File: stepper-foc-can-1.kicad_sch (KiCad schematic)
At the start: 60 parts, among them J1 TC2030, J2 Conn_01x02, J4 Conn_01x04_Pin, J5 Conn_01x02, J6 Conn_01x02, M1 Stepper_Motor_bipolar, SW1 SW_Push, SW2 SW_Push, SW3 SW_Push, U1 STM32G474RBTx, U2 MX25947, U3 TPS62933, U4 AS5047P, U9 TCAN3413, Y1 Crystal_GND24

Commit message: schem: run and fix ERC
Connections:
- net BTN1: now also U1.58 (PB5)
- no-connect marks 27 -> 26
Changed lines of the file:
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@@
 		(color 0 0 0 0)
 	)
+	(junction
+		(at 38.1 191.77)
+		(diameter 0)
+		(color 0 0 0 0)
+	)
 	(no_connect
 		(at 120.65 125.73)
@@
 		(at 85.09 72.39)
 	)
-	(no_connect
-		(at 120.65 110.49)
-	)
 	(wire
 		(pts
@@
 	(wire
 		(pts
-			(xy 34.29 191.77) (xy 40.64 191.77)
+			(xy 34.29 191.77) (xy 38.1 191.77)
 		)
 		(stroke
@@
 	(wire
 		(pts
+			(xy 130.81 110.49) (xy 120.65 110.49)
+		)
+		(stroke
+			(width 0)
+			(type default)
+		)
+	)
+	(wire
+		(pts
 			(xy 71.12 41.91) (xy 71.12 43.18)
 		)
@@
 	(wire
 		(pts
+			(xy 38.1 191.77) (xy 40.64 191.77)
+		)
+		(stroke
+			(width 0)
+			(type default)
+		)
+	)
+	(wire
+		(pts
 			(xy 74.93 85.09) (xy 85.09 85.09)
 		)
@@
 		)
 	)
+	(label "BTN1"
+		(at 130.81 110.49 180)
+		(effects
+			(font
+				(size 1.27 1.27)
+			)
+			(justify right bottom)
+		)
+	)
 	(label "IN2_A"
 		(at 166.37 78.74 0)
@@
 					(unit 1)
 				)
+			)
+		)
+	)
+	(symbol
+		(lib_id "power:PWR_FLAG")
+		(at 38.1 191.77 180)
+		(unit 1)
+		(body_style 1)
+		(exclude_from_sim no)
+		(in_bom yes)
+		(on_board yes)
+		(in_pos_files yes)
+		(dnp no)
+		(fields_autoplaced yes)
+		(property "Reference" "#FLG09"
+			(at 38.1 193.675 0)
+			(hide yes)
+			(show_name no)
+			(do_not_autoplace no)
+			(effects
+				(font
+					(size 1.27 1.27)
+				)
+			)
+		)
+		(property "Value" "PWR_FLAG"
+			(at 38.1 196.85 0)
+			(hide yes)
+			(show_name no)
+			(do_not_autoplace no)
+			(effects
+				(font
+					(size 1.27 1.27)
+				)
+			)
+		)
+		(property "Footprint" ""
+			(at 38.1 191.77 0)
+			(hide yes)
+			(show_name no)
+			(do_not_autoplace no)
+			(effects
+				(font
+					(size 1.27 1.27)
+				)
+			)
+		)
+		(property "Datasheet" ""
+			(at 38.1 191.77 0)
+			(hide yes)
+			(show_name no)
+			(do_not_autoplace no)
+			(effects
+				(font
+					(size 1.27 1.27)
+				)
+			)
+		)
+		(property "Description" "Special symbol for telling ERC where power comes from"
+			(at 38.1 191.77 0)
+			(hide yes)
+			(show_name no)
+			(do_not_autoplace no)
+			(effects
+				(font
+					(size 1.27 1.27)
+				)
+			)
+		)
+		(pin "1"
+		)
+		(instances
+			(project "stepper-foc-can-1"
+				(path "/7e511d2f-8abe-4907-a647-133ba6c8a8df"
+					(reference "#FLG09")
+					(unit 1)
+				)

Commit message: schem: add missing footprints
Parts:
- M1: footprint (none) -> Connector_JST:JST_XH_S4B-XH-A_1x04_P2.50mm_Horizontal
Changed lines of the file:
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@@
 			)
 		)
-		(property "Footprint" ""
+		(property "Footprint" "Connector_JST:JST_XH_S4B-XH-A_1x04_P2.50mm_Horizontal"
 			(at 204.724 78.486 0)
 			(hide yes)

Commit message: schem: add ordering info to BOM
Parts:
- M1: now left out of the parts list
- U1: Basic (none) -> X; JLCPCB Part # (none) -> C1235414; Manufacturer (none) -> STMicroelectronics; Manufacturer Part Number (none) -> STM32G474RBT3
- U2: Basic (none) -> X; JLCPCB Part # (none) -> C5875698; Manufacturer (none) -> Wuxi Maxinmicro; Manufacturer Part Number (none) -> MX25947ES
- U4: Basic (none) -> X; JLCPCB Part # (none) -> C962063; Manufacturer (none) -> AMS; Manufacturer Part Number (none) -> AS5047P-ATSM

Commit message: schem: add title
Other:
- company: (none) -> Rémi Ait-Younes
- title: (none) -> Stepper FOC CAN 1
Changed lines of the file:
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@@
 	(generator_version "10.0")
 	(paper "A4")
+	(title_block
+		(title "Stepper FOC CAN 1")
+		(date "2026-04-11")
+		(rev "01")
+		(company "Rémi Ait-Younes")
+	)
 	(rectangle
 		(start 233.68 82.55)

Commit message: schem: reannotate
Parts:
- renumbered C3 to C1, C15 to C10, C12 to C11, C13 to C12, C14 to C13, C17 to C14, C16 to C15, C1 to C16, C2 to C17, C6 to C2, C29 to C24, C30 to C25, C24 to C26, C4 to C3, C5 to C4, C7 to C5, C9 to C6, C10 to C7, C11 to C9, D11 to D6, J4 to J3, J5 to J4, J6 to J5, JP2 to JP1, R5 to R3, R8 to R4, R4 to R5, R9 to R6, R10 to R7, R11 to R8, R13 to R9, TP4 to TP1, U9 to U4, U4 to U5

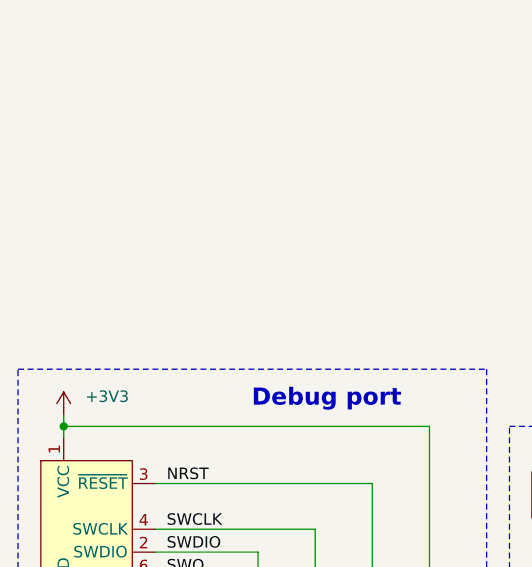
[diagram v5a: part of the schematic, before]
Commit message: schem: add mounting holes
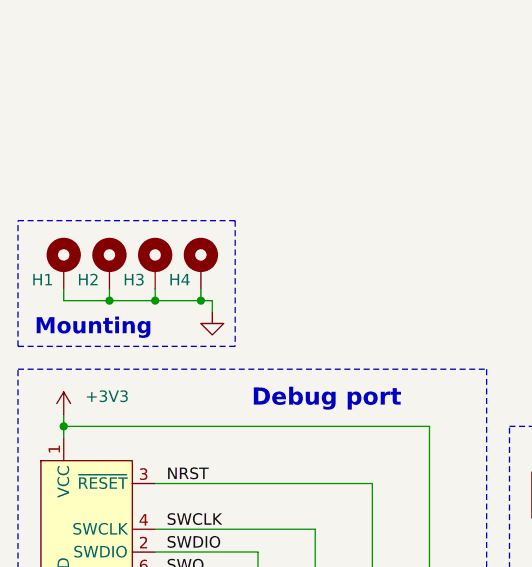
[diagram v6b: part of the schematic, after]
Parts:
- added H1, H2, H3, H4: MountingHole_Pad, MountingHole:MountingHole_3.2mm_M3_Pad_Via, symbol Mechanical:MountingHole_Pad
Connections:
- net GND: now also H1.1, H2.1, H3.1, H4.1
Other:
- note added: "Mounting"

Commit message: schem: update mounting holes footprint
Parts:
- H1, H2, H3, H4: footprint MountingHole:MountingHole_3.2mm_M3_Pad_Via -> MountingHole:MountingHole_3.2mm_M3_ISO7380_Pad
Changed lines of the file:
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@@
 			)
 		)
-		(property "Footprint" "MountingHole:MountingHole_3.2mm_M3_Pad_Via"
+		(property "Footprint" "MountingHole:MountingHole_3.2mm_M3_ISO7380_Pad"
 			(at 34.29 147.32 0)
 			(hide yes)
@@
 			)
 		)
-		(property "Footprint" "MountingHole:MountingHole_3.2mm_M3_Pad_Via"
+		(property "Footprint" "MountingHole:MountingHole_3.2mm_M3_ISO7380_Pad"
 			(at 19.05 147.32 0)
 			(hide yes)
@@
 			)
 		)
-		(property "Footprint" "MountingHole:MountingHole_3.2mm_M3_Pad_Via"
+		(property "Footprint" "MountingHole:MountingHole_3.2mm_M3_ISO7380_Pad"
 			(at 29.21 147.32 0)
 			(hide yes)
@@
 			)
 		)
-		(property "Footprint" "MountingHole:MountingHole_3.2mm_M3_Pad_Via"
+		(property "Footprint" "MountingHole:MountingHole_3.2mm_M3_ISO7380_Pad"
 			(at 24.13 147.32 0)
 			(hide yes)

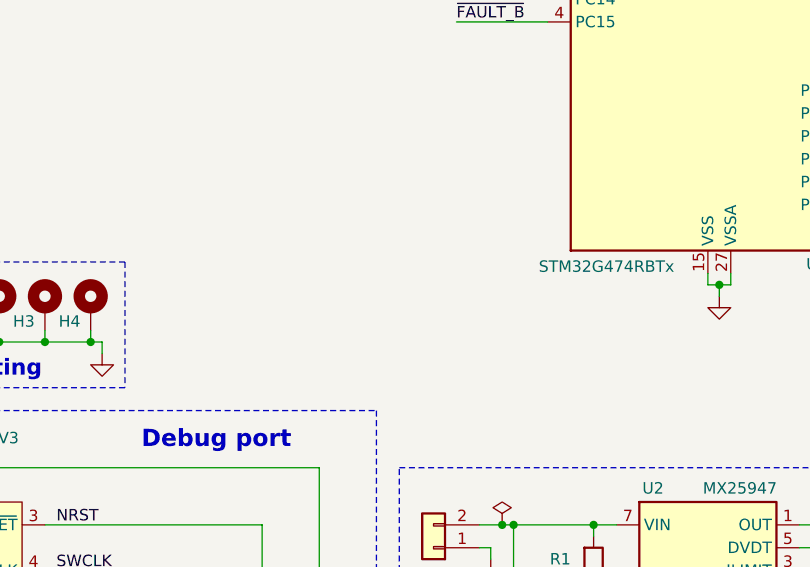
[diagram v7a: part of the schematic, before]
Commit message: pcb: add drvs placement
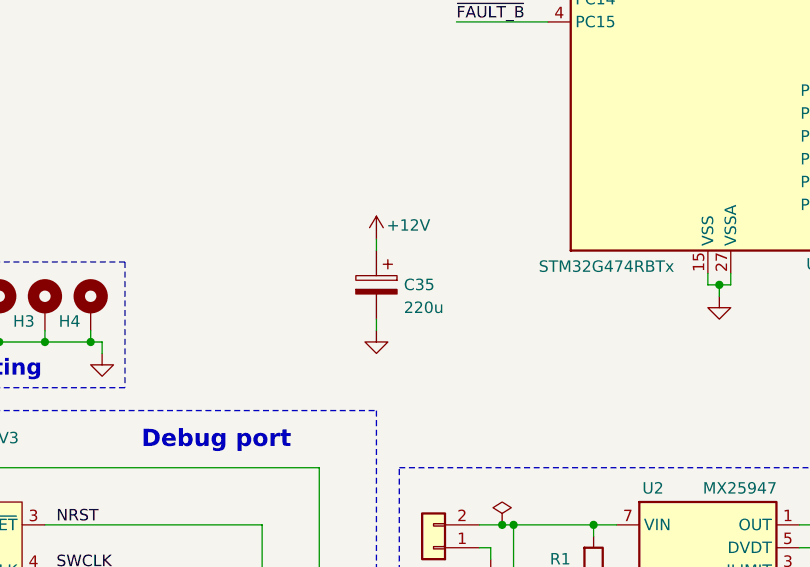
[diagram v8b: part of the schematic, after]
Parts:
- added C35: 220u, Capacitor_SMD:CP_Elec_6.3x7.7, symbol Device:C_Polarized
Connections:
- net +12V: now also C35.1
- net GND: now also C35.2
